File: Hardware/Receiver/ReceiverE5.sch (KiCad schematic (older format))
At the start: 37 parts, among them J1 KBUS, J2 AVR-PDI-6A, J3 CONN_01X08, J4 CONN_01X06, J5 CONN_01X06, J6 CONN_01X04, J7 CONN_01X04, U1 ATXMEGA32E5-A, U2 LM2731, U3 SN74LV07A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

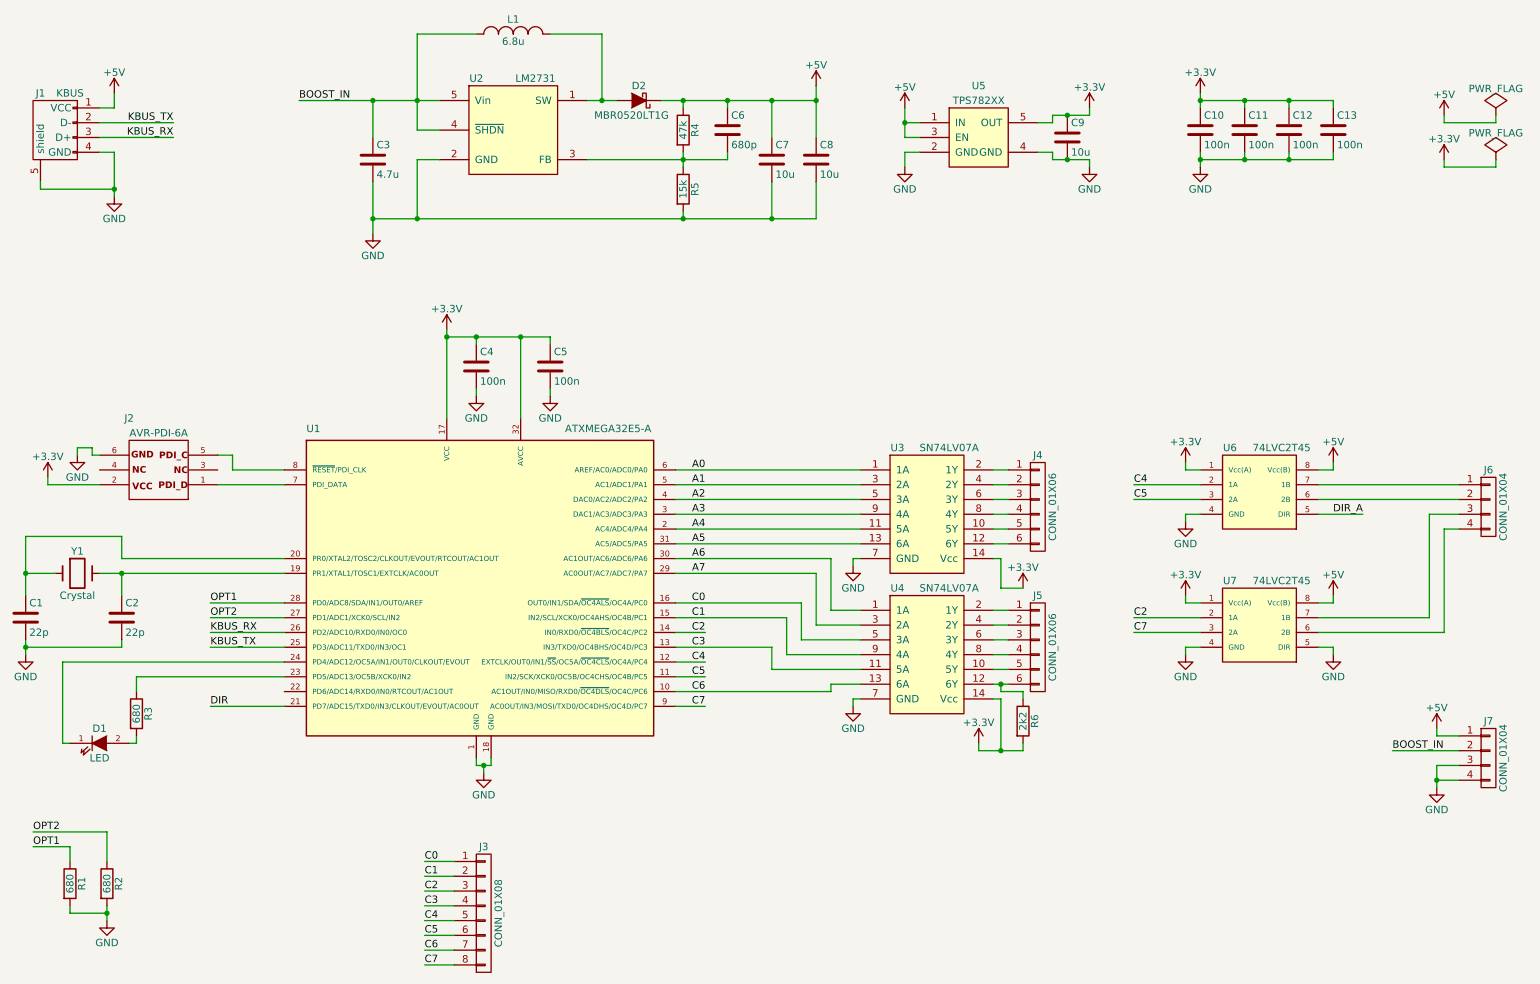
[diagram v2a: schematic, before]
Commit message: Fixed a few minor schematic errors
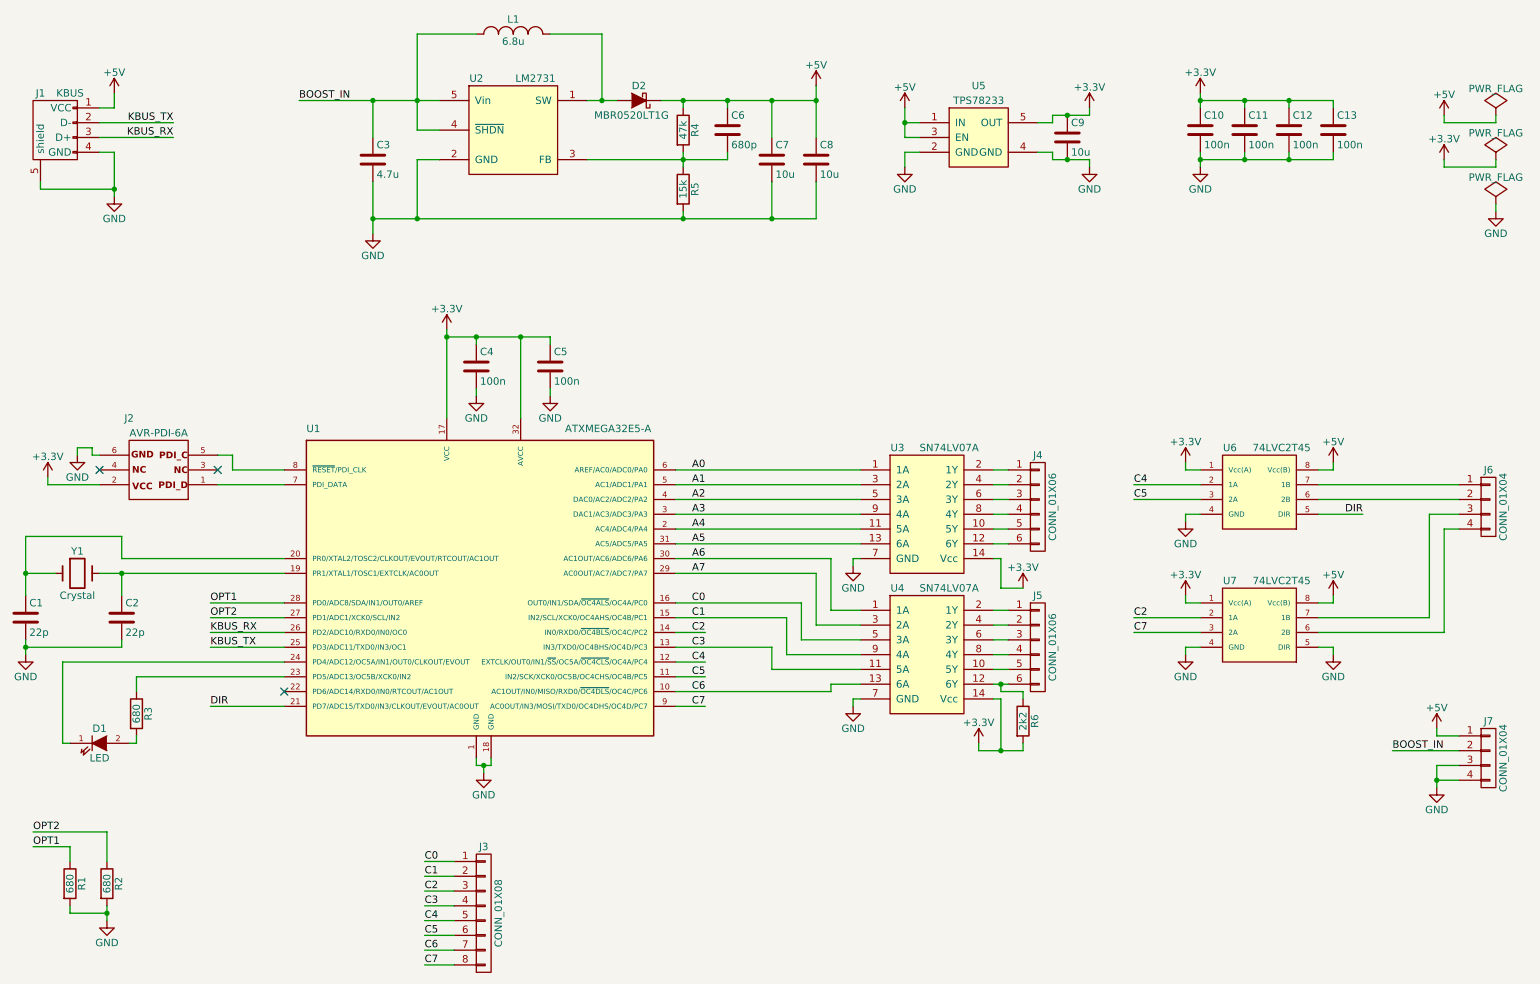
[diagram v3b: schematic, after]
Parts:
- U5: value TPS782XX -> TPS78233
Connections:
- net DIR_A is gone; now on net DIR: U6.5 (DIR)
- no-connect marks 0 -> 3
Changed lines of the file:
@@
 $EndComp
 $Comp
-L +5V #PWR12
+L +5V #PWR01
 U 1 1 582469D6
 P 6100 1150
-F 0 "#PWR12" H 6100 1000 50  0001 C CNN
+F 0 "#PWR01" H 6100 1000 50  0001 C CNN
 F 1 "+5V" H 6100 1290 50  0000 C CNN
 F 2 "" H 6100 1150 50  0000 C CNN
@@
 $EndComp
 $Comp
-L GND #PWR7
+L GND #PWR02
 U 1 1 582469FA
 P 3100 2150
-F 0 "#PWR7" H 3100 1900 50  0001 C CNN
+F 0 "#PWR02" H 3100 1900 50  0001 C CNN
 F 1 "GND" H 3100 2000 50  0000 C CNN
 F 2 "" H 3100 2150 50  0000 C CNN
@@
 $EndComp
 $Comp
-L PWR_FLAG #FLG1
+L PWR_FLAG #FLG03
 U 1 1 58246A8F
 P 10700 1350
-F 0 "#FLG1" H 10700 1445 50  0001 C CNN
+F 0 "#FLG03" H 10700 1445 50  0001 C CNN
 F 1 "PWR_FLAG" H 10700 1530 50  0000 C CNN
 F 2 "" H 10700 1350 50  0000 C CNN
@@
 $EndComp
 $Comp
-L +5V #PWR32
+L +5V #PWR04
 U 1 1 58246B44
 P 10350 1350
-F 0 "#PWR32" H 10350 1200 50  0001 C CNN
+F 0 "#PWR04" H 10350 1200 50  0001 C CNN
 F 1 "+5V" H 10350 1490 50  0000 C CNN
 F 2 "" H 10350 1350 50  0000 C CNN
@@
 $EndComp
 $Comp
-L +5V #PWR5
+L +5V #PWR05
 U 1 1 5824886A
 P 1350 1200
-F 0 "#PWR5" H 1350 1050 50  0001 C CNN
+F 0 "#PWR05" H 1350 1050 50  0001 C CNN
 F 1 "+5V" H 1350 1340 50  0000 C CNN
 F 2 "" H 1350 1200 50  0000 C CNN
@@
 $EndComp
 $Comp
-L GND #PWR6
+L GND #PWR06
 U 1 1 582489D4
 P 1350 1900
-F 0 "#PWR6" H 1350 1650 50  0001 C CNN
+F 0 "#PWR06" H 1350 1650 50  0001 C CNN
 F 1 "GND" H 1350 1750 50  0000 C CNN
 F 2 "" H 1350 1900 50  0000 C CNN
@@
 P 7200 1500
 F 0 "U5" H 7200 1850 50  0000 C CNN
-F 1 "TPS782XX" H 7200 1750 50  0000 C CNN
+F 1 "TPS78233" H 7200 1750 50  0000 C CNN
 F 2 "TO_SOT_Packages_SMD:SOT-23-5" H 7200 1250 50  0001 C CNN
 F 3 "" H 7200 1500 60  0000 C CNN
@@
 $EndComp
 $Comp
-L +5V #PWR15
+L +5V #PWR07
 U 1 1 5824ABA7
 P 6700 1300
-F 0 "#PWR15" H 6700 1150 50  0001 C CNN
+F 0 "#PWR07" H 6700 1150 50  0001 C CNN
 F 1 "+5V" H 6700 1440 50  0000 C CNN
 F 2 "" H 6700 1300 50  0000 C CNN
@@
 $EndComp
 $Comp
-L GND #PWR16
+L GND #PWR08
 U 1 1 5824AD24
 P 6700 1700
-F 0 "#PWR16" H 6700 1450 50  0001 C CNN
+F 0 "#PWR08" H 6700 1450 50  0001 C CNN
 F 1 "GND" H 6700 1550 50  0000 C CNN
 F 2 "" H 6700 1700 50  0000 C CNN
@@
 $EndComp
 $Comp
-L GND #PWR20
+L GND #PWR09
 U 1 1 5824B020
 P 7950 1700
-F 0 "#PWR20" H 7950 1450 50  0001 C CNN
+F 0 "#PWR09" H 7950 1450 50  0001 C CNN
 F 1 "GND" H 7950 1550 50  0000 C CNN
 F 2 "" H 7950 1700 50  0000 C CNN
@@
 $EndComp
 $Comp
-L +3.3V #PWR19
+L +3.3V #PWR010
 U 1 1 5824B213
 P 7950 1300
-F 0 "#PWR19" H 7950 1150 50  0001 C CNN
+F 0 "#PWR010" H 7950 1150 50  0001 C CNN
 F 1 "+3.3V" H 7950 1440 50  0000 C CNN
 F 2 "" H 7950 1300 50  0000 C CNN
@@
 $EndComp
 $Comp
-L +3.3V #PWR33
+L +3.3V #PWR011
 U 1 1 5824C026
 P 10350 1650
-F 0 "#PWR33" H 10350 1500 50  0001 C CNN
+F 0 "#PWR011" H 10350 1500 50  0001 C CNN
 F 1 "+3.3V" H 10350 1790 50  0000 C CNN
 F 2 "" H 10350 1650 50  0000 C CNN
@@
 $EndComp
 $Comp
-L PWR_FLAG #FLG2
+L PWR_FLAG #FLG012
 U 1 1 5824C328
 P 10700 1650
-F 0 "#FLG2" H 10700 1745 50  0001 C CNN
+F 0 "#FLG012" H 10700 1745 50  0001 C CNN
 F 1 "PWR_FLAG" H 10700 1830 50  0000 C CNN
 F 2 "" H 10700 1650 50  0000 C CNN
@@
 $EndComp
 $Comp
-L GND #PWR13
+L GND #PWR013
 U 1 1 5824EEE6
 P 6350 4400
-F 0 "#PWR13" H 6350 4150 50  0001 C CNN
+F 0 "#PWR013" H 6350 4150 50  0001 C CNN
 F 1 "GND" H 6350 4250 50  0000 C CNN
 F 2 "" H 6350 4400 50  0000 C CNN
@@
 $EndComp
 $Comp
-L GND #PWR14
+L GND #PWR014
 U 1 1 5824F2F5
 P 6350 5350
-F 0 "#PWR14" H 6350 5100 50  0001 C CNN
+F 0 "#PWR014" H 6350 5100 50  0001 C CNN
 F 1 "GND" H 6350 5200 50  0000 C CNN
 F 2 "" H 6350 5350 50  0000 C CNN
@@
 C5
 $Comp
-L GND #PWR22
+L GND #PWR015
 U 1 1 58251C44
 P 8600 4100
-F 0 "#PWR22" H 8600 3850 50  0001 C CNN
+F 0 "#PWR015" H 8600 3850 50  0001 C CNN
 F 1 "GND" H 8600 3950 50  0000 C CNN
 F 2 "" H 8600 4100 50  0000 C CNN
@@
 $EndComp
 $Comp
-L GND #PWR24
+L GND #PWR016
 U 1 1 58251C82
 P 8600 5000
-F 0 "#PWR24" H 8600 4750 50  0001 C CNN
+F 0 "#PWR016" H 8600 4750 50  0001 C CNN
 F 1 "GND" H 8600 4850 50  0000 C CNN
 F 2 "" H 8600 5000 50  0000 C CNN
@@
 $EndComp
 $Comp
-L +3.3V #PWR21
+L +3.3V #PWR017
 U 1 1 582523F9
 P 8600 3700
-F 0 "#PWR21" H 8600 3550 50  0001 C CNN
+F 0 "#PWR017" H 8600 3550 50  0001 C CNN
 F 1 "+3.3V" H 8600 3840 50  0000 C CNN
 F 2 "" H 8600 3700 50  0000 C CNN
@@
 $EndComp
 $Comp
-L +3.3V #PWR23
+L +3.3V #PWR018
 U 1 1 58252575
 P 8600 4600
-F 0 "#PWR23" H 8600 4450 50  0001 C CNN
+F 0 "#PWR018" H 8600 4450 50  0001 C CNN
 F 1 "+3.3V" H 8600 4740 50  0000 C CNN
 F 2 "" H 8600 4600 50  0000 C CNN
@@
 $EndComp
 $Comp
-L +5V #PWR27
+L +5V #PWR019
 U 1 1 58253B37
 P 9600 3700
-F 0 "#PWR27" H 9600 3550 50  0001 C CNN
+F 0 "#PWR019" H 9600 3550 50  0001 C CNN
 F 1 "+5V" H 9600 3840 50  0000 C CNN
 F 2 "" H 9600 3700 50  0000 C CNN
@@
 $EndComp
 $Comp
-L GND #PWR29
+L GND #PWR020
 U 1 1 58254196
 P 9600 5000
-F 0 "#PWR29" H 9600 4750 50  0001 C CNN
+F 0 "#PWR020" H 9600 4750 50  0001 C CNN
 F 1 "GND" H 9600 4850 50  0000 C CNN
 F 2 "" H 9600 5000 50  0000 C CNN
@@
 $EndComp
 $Comp
-L +5V #PWR28
+L +5V #PWR021
 U 1 1 582542A3
 P 9600 4600
-F 0 "#PWR28" H 9600 4450 50  0001 C CNN
+F 0 "#PWR021" H 9600 4450 50  0001 C CNN
 F 1 "+5V" H 9600 4740 50  0000 C CNN
 F 2 "" H 9600 4600 50  0000 C CNN
@@
 $EndComp
 Text Label 9800 4050 2    50   ~ 0
-DIR_A
+DIR
 Text Label 2000 5350 0    50   ~ 0
 DIR
@@
 $EndComp
 $Comp
-L +3.3V #PWR18
+L +3.3V #PWR022
 U 1 1 5825A872
 P 7500 4550
-F 0 "#PWR18" H 7500 4400 50  0001 C CNN
+F 0 "#PWR022" H 7500 4400 50  0001 C CNN
 F 1 "+3.3V" H 7500 4690 50  0000 C CNN
 F 2 "" H 7500 4550 50  0000 C CNN
@@
 $EndComp
 $Comp
-L +3.3V #PWR17
+L +3.3V #PWR023
 U 1 1 5825A961
 P 7200 5600
-F 0 "#PWR17" H 7200 5450 50  0001 C CNN
+F 0 "#PWR023" H 7200 5450 50  0001 C CNN
 F 1 "+3.3V" H 7200 5740 50  0000 C CNN
 F 2 "" H 7200 5600 50  0000 C CNN
@@
 $EndComp
 $Comp
-L +5V #PWR30
+L +5V #PWR024
 U 1 1 5825BCEC
 P 10300 5500
-F 0 "#PWR30" H 10300 5350 50  0001 C CNN
+F 0 "#PWR024" H 10300 5350 50  0001 C CNN
 F 1 "+5V" H 10300 5640 50  0000 C CNN
 F 2 "" H 10300 5500 50  0000 C CNN
@@
 $EndComp
 $Comp
-L GND #PWR31
+L GND #PWR025
 U 1 1 5825BEA2
 P 10300 5900
-F 0 "#PWR31" H 10300 5650 50  0001 C CNN
+F 0 "#PWR025" H 10300 5650 50  0001 C CNN
 F 1 "GND" H 10300 5750 50  0000 C CNN
 F 2 "" H 10300 5900 50  0000 C CNN
@@
 $EndComp
 $Comp
-L GND #PWR1
+L GND #PWR026
 U 1 1 5825FD90
 P 750 5000
-F 0 "#PWR1" H 750 4750 50  0001 C CNN
+F 0 "#PWR026" H 750 4750 50  0001 C CNN
 F 1 "GND" H 750 4850 50  0000 C CNN
 F 2 "" H 750 5000 50  0000 C CNN
@@
 $EndComp
 $Comp
-L GND #PWR3
+L GND #PWR027
 U 1 1 582615C7
 P 1100 3650
-F 0 "#PWR3" H 1100 3400 50  0001 C CNN
+F 0 "#PWR027" H 1100 3400 50  0001 C CNN
 F 1 "GND" H 1100 3500 50  0000 C CNN
 F 2 "" H 1100 3650 50  0000 C CNN
@@
 $EndComp
 $Comp
-L +3.3V #PWR2
+L +3.3V #PWR028
 U 1 1 582618AA
 P 900 3800
-F 0 "#PWR2" H 900 3650 50  0001 C CNN
+F 0 "#PWR028" H 900 3650 50  0001 C CNN
 F 1 "+3.3V" H 900 3940 50  0000 C CNN
 F 2 "" H 900 3800 50  0000 C CNN
@@
 $EndComp
 $Comp
-L +3.3V #PWR8
+L +3.3V #PWR029
 U 1 1 58261F69
 P 3600 2800
-F 0 "#PWR8" H 3600 2650 50  0001 C CNN
+F 0 "#PWR029" H 3600 2650 50  0001 C CNN
 F 1 "+3.3V" H 3600 2940 50  0000 C CNN
 F 2 "" H 3600 2800 50  0000 C CNN
@@
 $EndComp
 $Comp
-L GND #PWR9
+L GND #PWR030
 U 1 1 582625C0
 P 3800 3250
-F 0 "#PWR9" H 3800 3000 50  0001 C CNN
+F 0 "#PWR030" H 3800 3000 50  0001 C CNN
 F 1 "GND" H 3800 3100 50  0000 C CNN
 F 2 "" H 3800 3250 50  0000 C CNN
@@
 $EndComp
 $Comp
-L GND #PWR11
+L GND #PWR031
 U 1 1 58262CE9
 P 4300 3250
-F 0 "#PWR11" H 4300 3000 50  0001 C CNN
+F 0 "#PWR031" H 4300 3000 50  0001 C CNN
 F 1 "GND" H 4300 3100 50  0000 C CNN
 F 2 "" H 4300 3250 50  0000 C CNN
@@
 $EndComp
 $Comp
-L GND #PWR10
+L GND #PWR032
 U 1 1 58264117
 P 3850 5800
-F 0 "#PWR10" H 3850 5550 50  0001 C CNN
+F 0 "#PWR032" H 3850 5550 50  0001 C CNN
 F 1 "GND" H 3850 5650 50  0000 C CNN
 F 2 "" H 3850 5800 50  0000 C CNN
@@
 OPT2
 $Comp
-L GND #PWR4
+L GND #PWR033
 U 1 1 582674C6
 P 1300 6800
-F 0 "#PWR4" H 1300 6550 50  0001 C CNN
+F 0 "#PWR033" H 1300 6550 50  0001 C CNN
 F 1 "GND" H 1300 6650 50  0000 C CNN
 F 2 "" H 1300 6800 50  0000 C CNN
@@
 Connection ~ 6100 1250
 $Comp
-L +3.3V #PWR25
+L +3.3V #PWR034
 U 1 1 5827EBCB
 P 8700 1200
-F 0 "#PWR25" H 8700 1050 50  0001 C CNN
+F 0 "#PWR034" H 8700 1050 50  0001 C CNN
 F 1 "+3.3V" H 8700 1340 50  0000 C CNN
 F 2 "" H 8700 1200 50  0000 C CNN
@@
 Connection ~ 9000 1650
 $Comp
-L GND #PWR26
+L GND #PWR035
 U 1 1 5827F399
 P 8700 1700
-F 0 "#PWR26" H 8700 1450 50  0001 C CNN
+F 0 "#PWR035" H 8700 1450 50  0001 C CNN
 F 1 "GND" H 8700 1550 50  0000 C CNN
 F 2 "" H 8700 1700 50  0000 C CNN
@@
 Wire Wire Line
 	7350 4350 7300 4350
+NoConn ~ 2050 3750
+NoConn ~ 1250 3750
+NoConn ~ 2500 5250
+$Comp
+L PWR_FLAG #FLG036
+U 1 1 582B30DF
+P 10700 1950
+F 0 "#FLG036" H 10700 2045 50  0001 C CNN
+F 1 "PWR_FLAG" H 10700 2130 50  0000 C CNN
+F 2 "" H 10700 1950 50  0000 C CNN
+F 3 "" H 10700 1950 50  0000 C CNN
+	1    10700 1950
+	1    0    0    -1
+$EndComp
+$Comp
+L GND #PWR037
+U 1 1 582B3159
+P 10700 2000
+F 0 "#PWR037" H 10700 1750 50  0001 C CNN
+F 1 "GND" H 10700 1850 50  0000 C CNN
+F 2 "" H 10700 2000 50  0000 C CNN
+F 3 "" H 10700 2000 50  0000 C CNN
+	1    10700 2000
+	1    0    0    -1
+$EndComp
+Wire Wire Line
+	10700 2000 10700 1950
 $EndSCHEMATC

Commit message: Changed PDI header to 2.54mm pitch TH
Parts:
- J2: footprint kuro:3x2_1.27mm_SMD_header -> Pin_Headers:Pin_Header_Straight_2x03
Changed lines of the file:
@@
 F 0 "J2" H 1850 3400 50  0000 C CNN
 F 1 "AVR-PDI-6A" H 1650 3500 50  0000 C CNN
-F 2 "kuro:3x2_1.27mm_SMD_header" V 1100 3800 50  0001 C CNN
+F 2 "Pin_Headers:Pin_Header_Straight_2x03" V 1100 3800 50  0001 C CNN
 F 3 "" H 1650 3750 50  0000 C CNN
 	1    1650 3750
